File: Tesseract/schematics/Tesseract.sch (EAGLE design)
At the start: 109 parts, among them IC1 MC7805CDTG, IC2 NE5532D, IC3 NE5532D, IC4 QUAD_OPAMPD, IC5 LM4040B10, Q1 BSS123, Q2 SI2309CDS, Q3 BC846

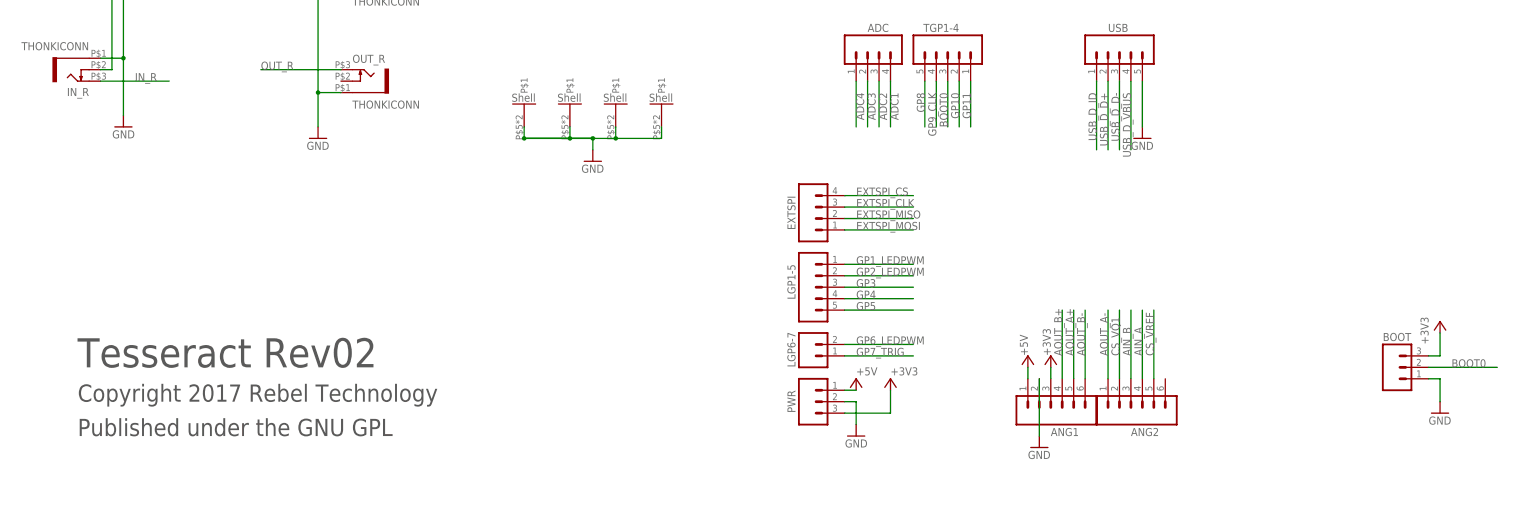
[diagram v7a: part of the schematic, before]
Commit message: added toggles
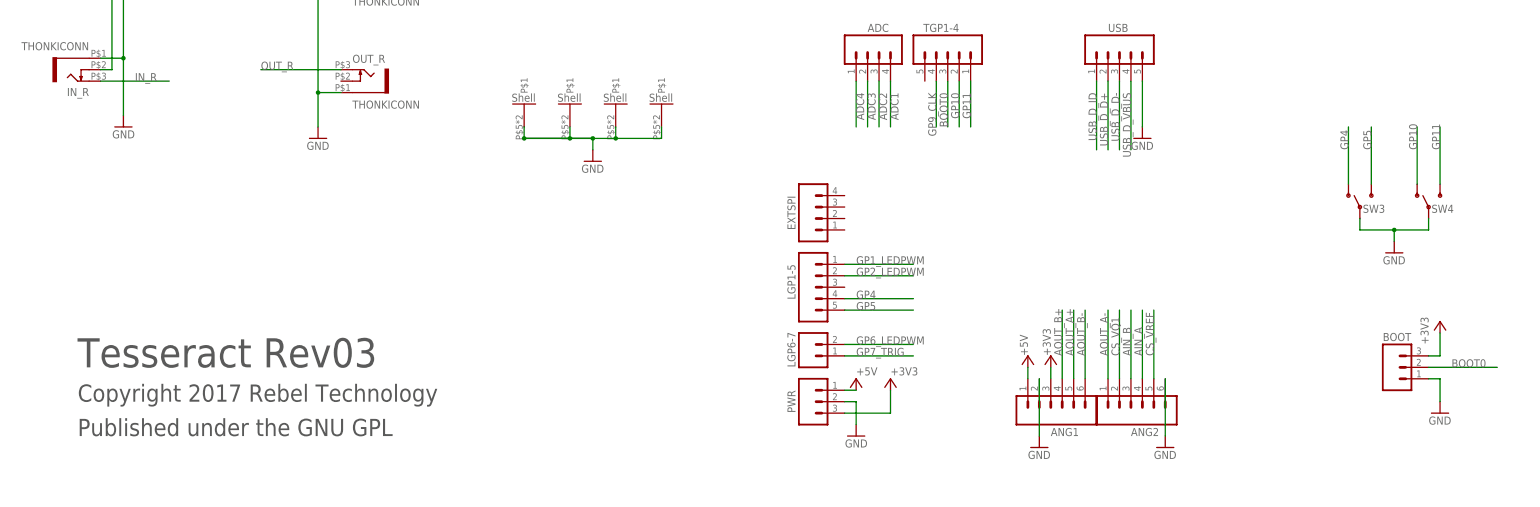
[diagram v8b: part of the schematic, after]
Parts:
- added SW3, SW4: SUB-MIN-SPDT, Rebel:SUB-MIN-SPDT
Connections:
- removed net EXTSPI_CLK: EXTSPI.3
- removed net EXTSPI_CS: EXTSPI.4
- removed net EXTSPI_MISO: EXTSPI.2
- removed net EXTSPI_MOSI: EXTSPI.1
- removed net GP3: LGP1-5.3
- removed net GP8: TGP1-4.5
- net GND: now also ANG2.6, SW3.P, SW4.P
- net GP10: now also SW4.O
- net GP11: now also SW4.S
- net GP4: now also SW3.O
- net GP5: now also SW3.S
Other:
- note added: "Tesseract Rev03"
- note removed: "Tesseract Rev02"
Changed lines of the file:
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@@
 <part name="LED1" library="Rebel" deviceset="MULTICOMP_703-1028" device=""/>
 <part name="R36" library="Rebel" deviceset="R-EU_" device="0603" value="1k"/>
+<part name="SW3" library="Rebel" deviceset="SUB-MIN-SPDT" device=""/>
+<part name="SW4" library="Rebel" deviceset="SUB-MIN-SPDT" device=""/>
+<part name="GND62" library="supply1" deviceset="GND" device=""/>
+<part name="GND3" library="supply1" deviceset="GND" device=""/>
 </parts>
 <sheets>
 <sheet>
 <plain>
-<text x="-66.04" y="-22.86" size="6.4516" layer="97" font="vector">Tesseract Rev02</text>
+<text x="-66.04" y="-22.86" size="6.4516" layer="97" font="vector">Tesseract Rev03</text>
 <text x="-66.04" y="-30.48" size="3.81" layer="97" font="vector">Copyright 2017 Rebel Technology</text>
 <text x="-66.04" y="-38.1" size="3.81" layer="97" font="vector">Published under the GNU GPL</text>
@@
 <instance part="LED1" gate="G$1" x="-58.42" y="198.12" rot="R90"/>
 <instance part="R36" gate="G$1" x="-40.64" y="139.7" rot="MR180"/>
+<instance part="SW3" gate="G$1" x="218.44" y="12.7" smashed="yes" rot="R90">
+<attribute name="NAME" x="219.075" y="11.43" size="1.778" layer="95"/>
+</instance>
+<instance part="SW4" gate="G$1" x="233.68" y="12.7" smashed="yes" rot="R90">
+<attribute name="NAME" x="234.315" y="11.43" size="1.778" layer="95"/>
+</instance>
+<instance part="GND62" gate="1" x="226.06" y="2.54"/>
+<instance part="GND3" gate="1" x="175.26" y="-40.64"/>
 </instances>
 <busses>
@@
 <wire x1="195.58" y1="83.82" x2="195.58" y2="86.36" width="0.1524" layer="91"/>
 </segment>
+<segment>
+<pinref part="GND62" gate="1" pin="GND"/>
+<wire x1="218.44" y1="7.62" x2="226.06" y2="7.62" width="0.1524" layer="91"/>
+<wire x1="226.06" y1="7.62" x2="233.68" y2="7.62" width="0.1524" layer="91"/>
+<wire x1="226.06" y1="5.08" x2="226.06" y2="7.62" width="0.1524" layer="91"/>
+<junction x="226.06" y="7.62"/>
+<pinref part="SW4" gate="G$1" pin="P"/>
+<wire x1="233.68" y1="10.16" x2="233.68" y2="7.62" width="0.1524" layer="91"/>
+<pinref part="SW3" gate="G$1" pin="P"/>
+<wire x1="218.44" y1="10.16" x2="218.44" y2="7.62" width="0.1524" layer="91"/>
+</segment>
+<segment>
+<pinref part="ANG2" gate="G$1" pin="6"/>
+<pinref part="GND3" gate="1" pin="GND"/>
+<wire x1="175.26" y1="-25.4" x2="175.26" y2="-38.1" width="0.1524" layer="91"/>
+</segment>
 </net>
 <net name="+5V" class="0">
@@
 <wire x1="167.64" y1="195.58" x2="167.64" y2="208.28" width="0.1524" layer="91"/>
 <junction x="167.64" y="208.28"/>
-</segment>
-</net>
-<net name="EXTSPI_CS" class="0">
-<segment>
-<pinref part="EXTSPI" gate="G$1" pin="4"/>
-<wire x1="104.14" y1="15.24" x2="119.38" y2="15.24" width="0.1524" layer="91"/>
-<label x="106.68" y="15.24" size="1.778" layer="95"/>
-</segment>
-</net>
-<net name="EXTSPI_MOSI" class="0">
-<segment>
-<pinref part="EXTSPI" gate="G$1" pin="1"/>
-<wire x1="104.14" y1="7.62" x2="119.38" y2="7.62" width="0.1524" layer="91"/>
-<label x="106.68" y="7.62" size="1.778" layer="95"/>
-</segment>
-</net>
-<net name="EXTSPI_CLK" class="0">
-<segment>
-<pinref part="EXTSPI" gate="G$1" pin="3"/>
-<wire x1="104.14" y1="12.7" x2="119.38" y2="12.7" width="0.1524" layer="91"/>
-<label x="106.68" y="12.7" size="1.778" layer="95"/>
-</segment>
-</net>
-<net name="EXTSPI_MISO" class="0">
-<segment>
-<wire x1="104.14" y1="10.16" x2="119.38" y2="10.16" width="0.1524" layer="91"/>
-<label x="106.68" y="10.16" size="1.778" layer="95"/>
-<pinref part="EXTSPI" gate="G$1" pin="2"/>
 </segment>
 </net>
@@
 <pinref part="TGP1-4" gate="G$1" pin="2"/>
 </segment>
-</net>
-<net name="GP8" class="0">
-<segment>
-<wire x1="121.92" y1="40.64" x2="121.92" y2="30.48" width="0.1524" layer="91"/>
-<label x="121.92" y="38.1" size="1.778" layer="95" rot="MR270"/>
-<pinref part="TGP1-4" gate="G$1" pin="5"/>
+<segment>
+<wire x1="231.14" y1="17.78" x2="231.14" y2="30.48" width="0.1524" layer="91"/>
+<label x="231.14" y="25.4" size="1.778" layer="95" rot="R90"/>
+<pinref part="SW4" gate="G$1" pin="O"/>
 </segment>
 </net>
@@
 <label x="106.68" y="-10.16" size="1.778" layer="95"/>
 </segment>
+<segment>
+<wire x1="220.98" y1="17.78" x2="220.98" y2="30.48" width="0.1524" layer="91"/>
+<label x="220.98" y="25.4" size="1.778" layer="95" rot="R90"/>
+<pinref part="SW3" gate="G$1" pin="S"/>
+</segment>
 </net>
 <net name="GP4" class="0">
@@
 <label x="106.68" y="-7.62" size="1.778" layer="95"/>
 </segment>
-</net>
-<net name="GP3" class="0">
-<segment>
-<pinref part="LGP1-5" gate="G$1" pin="3"/>
-<wire x1="104.14" y1="-5.08" x2="119.38" y2="-5.08" width="0.1524" layer="91"/>
-<label x="106.68" y="-5.08" size="1.778" layer="95"/>
+<segment>
+<wire x1="215.9" y1="17.78" x2="215.9" y2="30.48" width="0.1524" layer="91"/>
+<label x="215.9" y="25.4" size="1.778" layer="95" rot="R90"/>
+<pinref part="SW3" gate="G$1" pin="O"/>
 </segment>
 </net>
@@
 <label x="132.08" y="38.1" size="1.778" layer="95" rot="MR270"/>
 </segment>
-</net>
+<segment>
+<wire x1="236.22" y1="30.48" x2="236.22" y2="17.78" width="0.1524" layer="91"/>
+<label x="236.22" y="25.4" size="1.778" layer="95" rot="R90"/>
+<pinref part="SW4" gate="G$1" pin="S"/>
+</segment>
+</net>
